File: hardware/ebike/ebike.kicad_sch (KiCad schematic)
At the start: 0 parts

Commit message: decoupling caps for STM
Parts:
- added C1, C2, C3, C7: 100n, symbol Device:C
- added C10, C9: 15p, symbol Device:C
- added C4: 4.7u, symbol Device:C
- added C5: 10n, symbol Device:C
- added C6, C8: 1u, symbol Device:C
- added FB1: 47, symbol Device:FerriteBead
- added U1: STM32G431CBTx, Package_QFP:LQFP-48_7x7mm_P0.5mm, symbol MCU_ST_STM32G4:STM32G431CBTx
- added Y1: ABLS-8MHZ-B2-T, E-Bike Footprints:XTAL_ABLS-8.000MHZ-B2-T, symbol Device:Crystal
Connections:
- new net: C5.1, C6.1, FB1.2
- new net: C10.1, U1.6 (PF1), Y1.2
- new net: C9.1, U1.5 (PF0), Y1.1
- new net +3.3V: C1.1, C2.1, C3.1, C4.1, C7.1, C8.1, FB1.1, U1.1 (VBAT), U1.20 (VREF+), U1.21 (VDDA), U1.24 (VDD), U1.36 (VDD), U1.48 (VDD)
- new net GND: C1.2, C10.2, C2.2, C3.2, C4.2, C5.2, C6.2, C7.2, C8.2, C9.2, U1.19 (VSSA), U1.23 (VSS), U1.35 (VSS), U1.47 (VSS)
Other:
- added sheet Battery Management (batteryman.kicad_sch)
- added sheet Motor Control (motor.kicad_sch)
- added sheet Peripherals (peripherals.kicad_sch)

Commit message: started on power management
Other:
- sheet Battery Management renamed Power Control
- added sheet Battery Control (battery_control.kicad_sch)
- sheet Power Control: file batteryman.kicad_sch -> power.kicad_sch
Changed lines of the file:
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@@
+	)
+	(sheet
+		(at 21.59 91.44)
+		(size 29.21 12.7)
+		(exclude_from_sim no)
+		(in_bom yes)
+		(on_board yes)
+		(dnp no)
+		(fields_autoplaced yes)
+		(stroke
+			(width 0.1524)
+			(type solid)
+		)
+		(fill
+			(color 0 0 0 0.0000)
+		)
+		(property "Sheetname" "Battery Control"
+			(at 21.59 90.7284 0)
+			(effects
+				(font
+					(size 1.27 1.27)
+				)
+				(justify left bottom)
+			)
+		)
+		(property "Sheetfile" "battery_control.kicad_sch"
+			(at 21.59 104.7246 0)
+			(effects
+				(font
+					(size 1.27 1.27)
+				)
+				(justify left top)
+			)
+		)
+		(instances
+			(project "ebike"
+				(path "/fbe3366b-3e6e-4322-b4fc-2801645ea115"
+					(page "5")
+				)
+			)
+		)
 	)
 	(sheet
@@
 			(color 0 0 0 0.0000)
 		)
-		(property "Sheetname" "Battery Management"
+		(property "Sheetname" "Power Control"
 			(at 21.59 51.3584 0)
 			(effects
@@
 			)
 		)
-		(property "Sheetfile" "batteryman.kicad_sch"
+		(property "Sheetfile" "power.kicad_sch"
 			(at 21.59 65.3546 0)
 			(effects

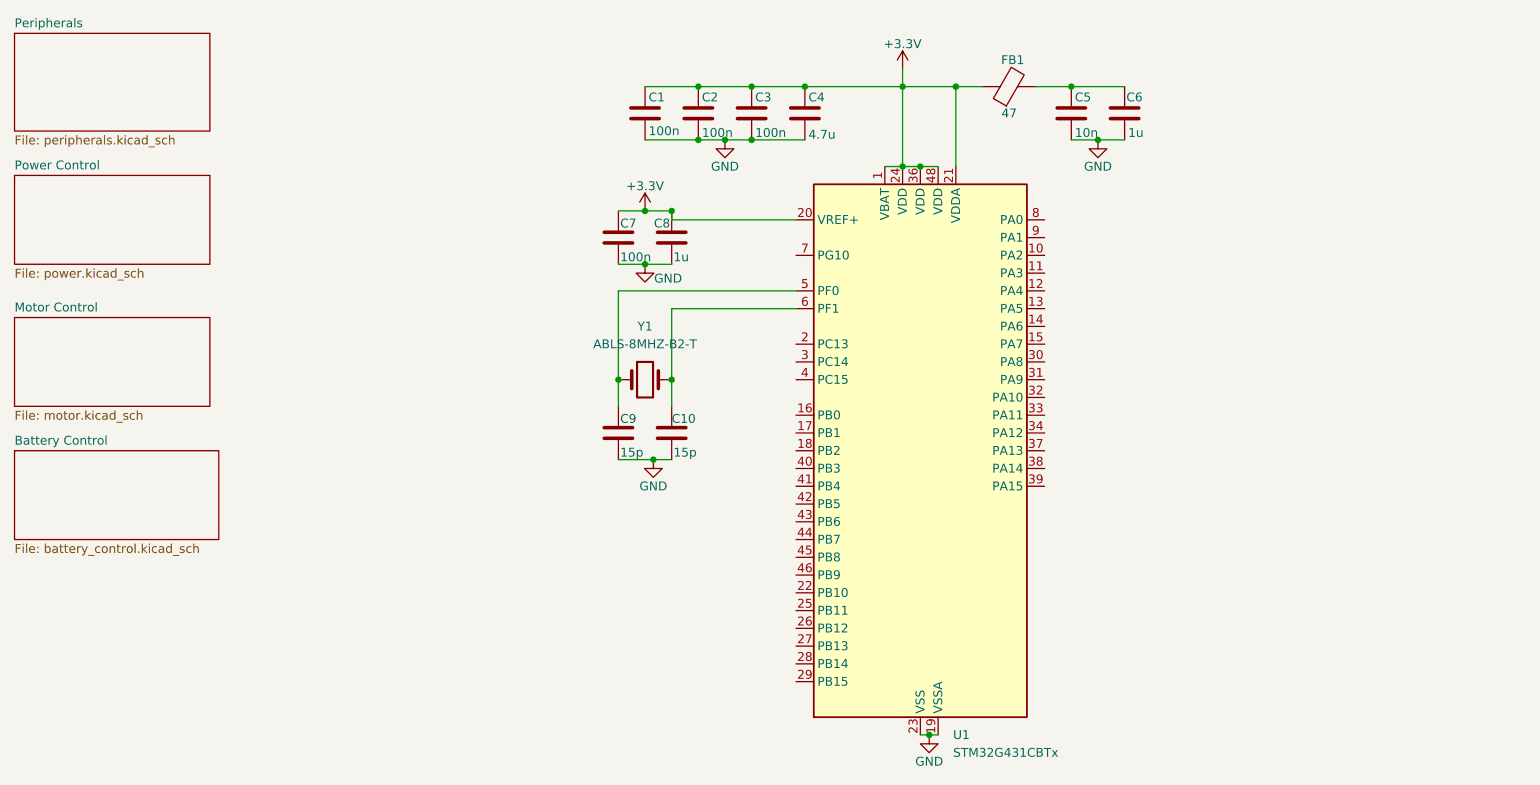
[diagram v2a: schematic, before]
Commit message: Wired PWM, ADC to MCU. Added HAL filtration + battery decoupling
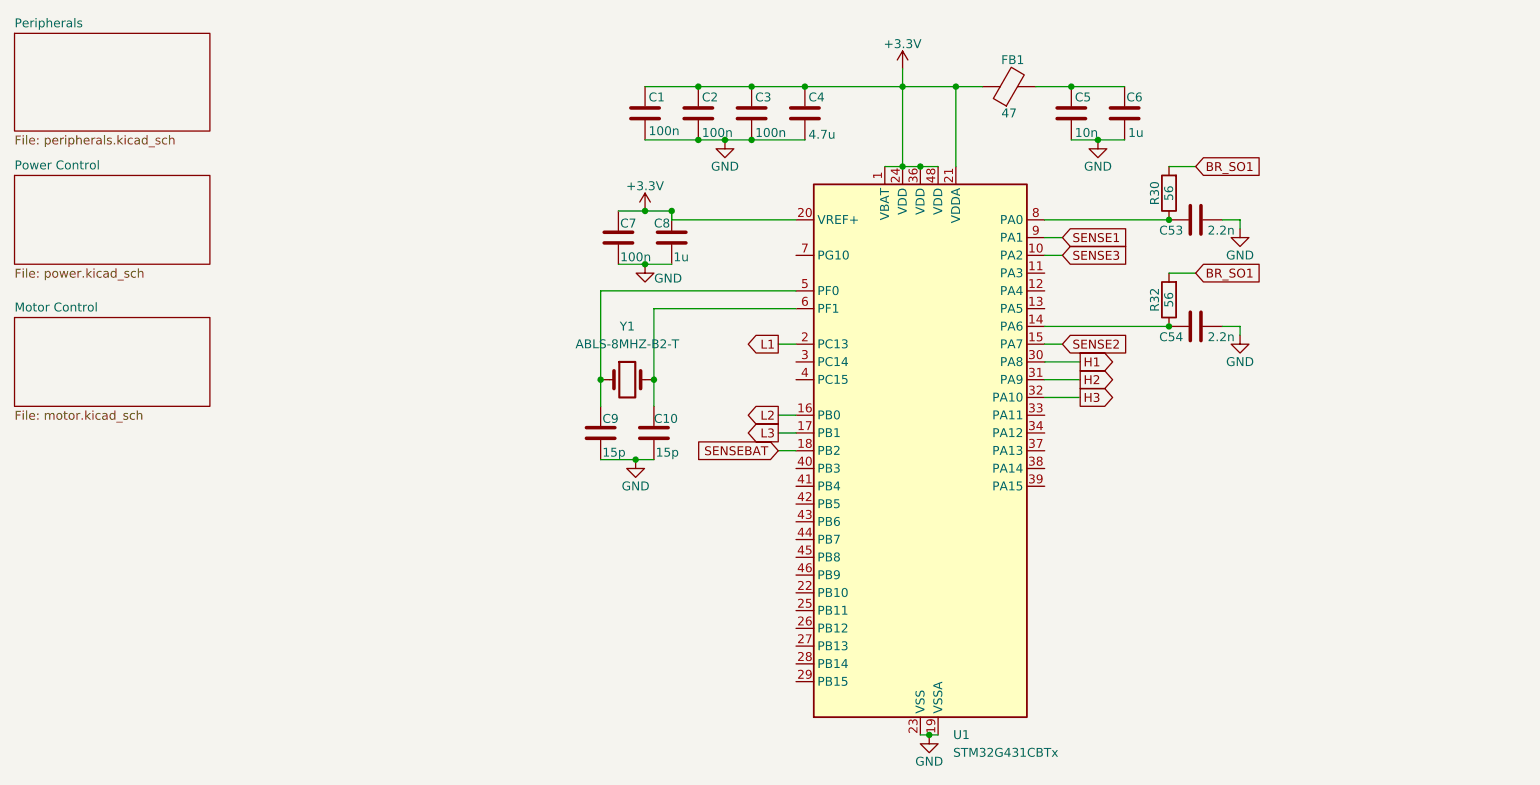
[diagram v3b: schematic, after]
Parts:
- added C53, C54: 2.2n, symbol Device:C
- added R30, R32: 56, symbol Device:R
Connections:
- net GND: now also C53.2, C54.2
- net SENSE3: now reaches U1.10 (PA2)
- net at U1.14 (PA6): now also C54.1, R32.1
- net SENSE2: now reaches U1.15 (PA7)
- net L2: now reaches U1.16 (PB0)
- net L3: now reaches U1.17 (PB1)
- net SENSEBAT: now reaches U1.18 (PB2)
- net L1: now reaches U1.2 (PC13)
- net H1: now reaches U1.30 (PA8)
- net H2: now reaches U1.31 (PA9)
- net H3: now reaches U1.32 (PA10)
- net at U1.8 (PA0): now also C53.1, R30.1
- net SENSE1: now reaches U1.9 (PA1)
- new net BR_SO1: R30.2, R32.2
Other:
- removed sheet Battery Control
- moved on the sheet: C10, C9, Y1

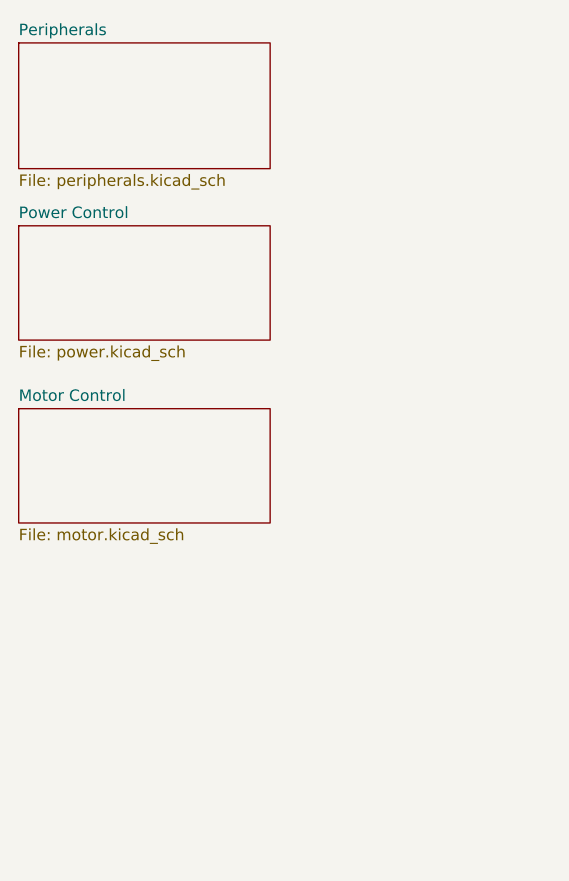
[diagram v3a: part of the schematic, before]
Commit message: wired most of peripherals
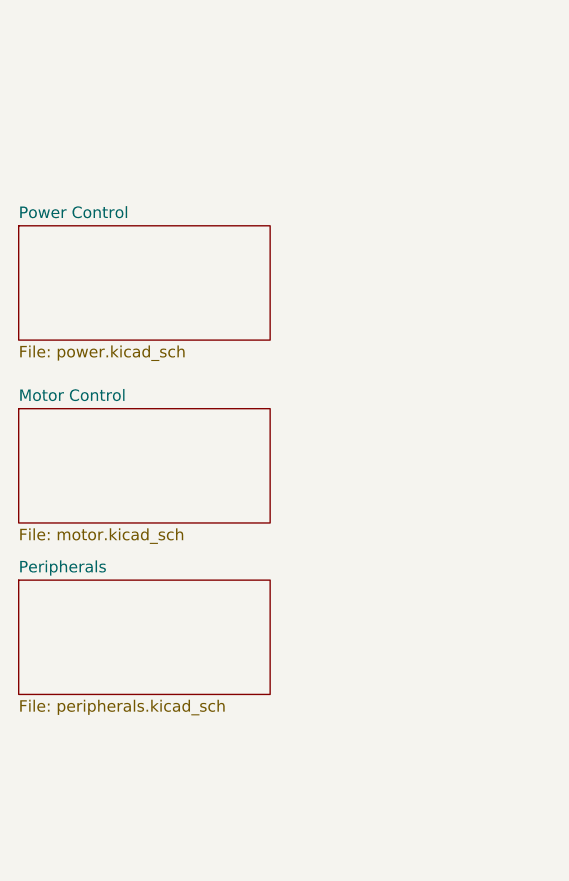
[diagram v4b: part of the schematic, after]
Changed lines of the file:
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@@
+	)
+	(sheet
+		(at 21.59 91.44)
+		(size 27.94 12.7)
+		(exclude_from_sim no)
+		(in_bom yes)
+		(on_board yes)
+		(dnp no)
+		(fields_autoplaced yes)
+		(stroke
+			(width 0.1524)
+			(type solid)
+		)
+		(fill
+			(color 0 0 0 0.0000)
+		)
+		(property "Sheetname" "Peripherals"
+			(at 21.59 90.7284 0)
+			(effects
+				(font
+					(size 1.27 1.27)
+				)
+				(justify left bottom)
+			)
+		)
+		(property "Sheetfile" "peripherals.kicad_sch"
+			(at 21.59 104.7246 0)
+			(effects
+				(font
+					(size 1.27 1.27)
+				)
+				(justify left top)
+			)
+		)
+		(instances
+			(project "ebike"
+				(path "/fbe3366b-3e6e-4322-b4fc-2801645ea115"
+					(page "4")
+				)
+			)
+		)
 	)
 	(sheet
@@
 			(project "ebike"
 				(path "/fbe3366b-3e6e-4322-b4fc-2801645ea115"
-					(page "4")
-				)
-			)
-		)
-	)
-	(sheet
-		(at 21.59 31.75)
-		(size 27.94 13.97)
-		(exclude_from_sim no)
-		(in_bom yes)
-		(on_board yes)
-		(dnp no)
-		(fields_autoplaced yes)
-		(stroke
-			(width 0.1524)
-			(type solid)
-		)
-		(fill
-			(color 0 0 0 0.0000)
-		)
-		(property "Sheetname" "Peripherals"
-			(at 21.59 31.0384 0)
-			(effects
-				(font
-					(size 1.27 1.27)
-				)
-				(justify left bottom)
-			)
-		)
-		(property "Sheetfile" "peripherals.kicad_sch"
-			(at 21.59 46.3046 0)
-			(effects
-				(font
-					(size 1.27 1.27)
-				)
-				(justify left top)
-			)
-		)
-		(instances
-			(project "ebike"
-				(path "/fbe3366b-3e6e-4322-b4fc-2801645ea115"
-					(page "2")
+					(page "3")
 				)
 			)
@@
 			(project "ebike"
 				(path "/fbe3366b-3e6e-4322-b4fc-2801645ea115"
-					(page "3")
+					(page "2")
 				)
 			)

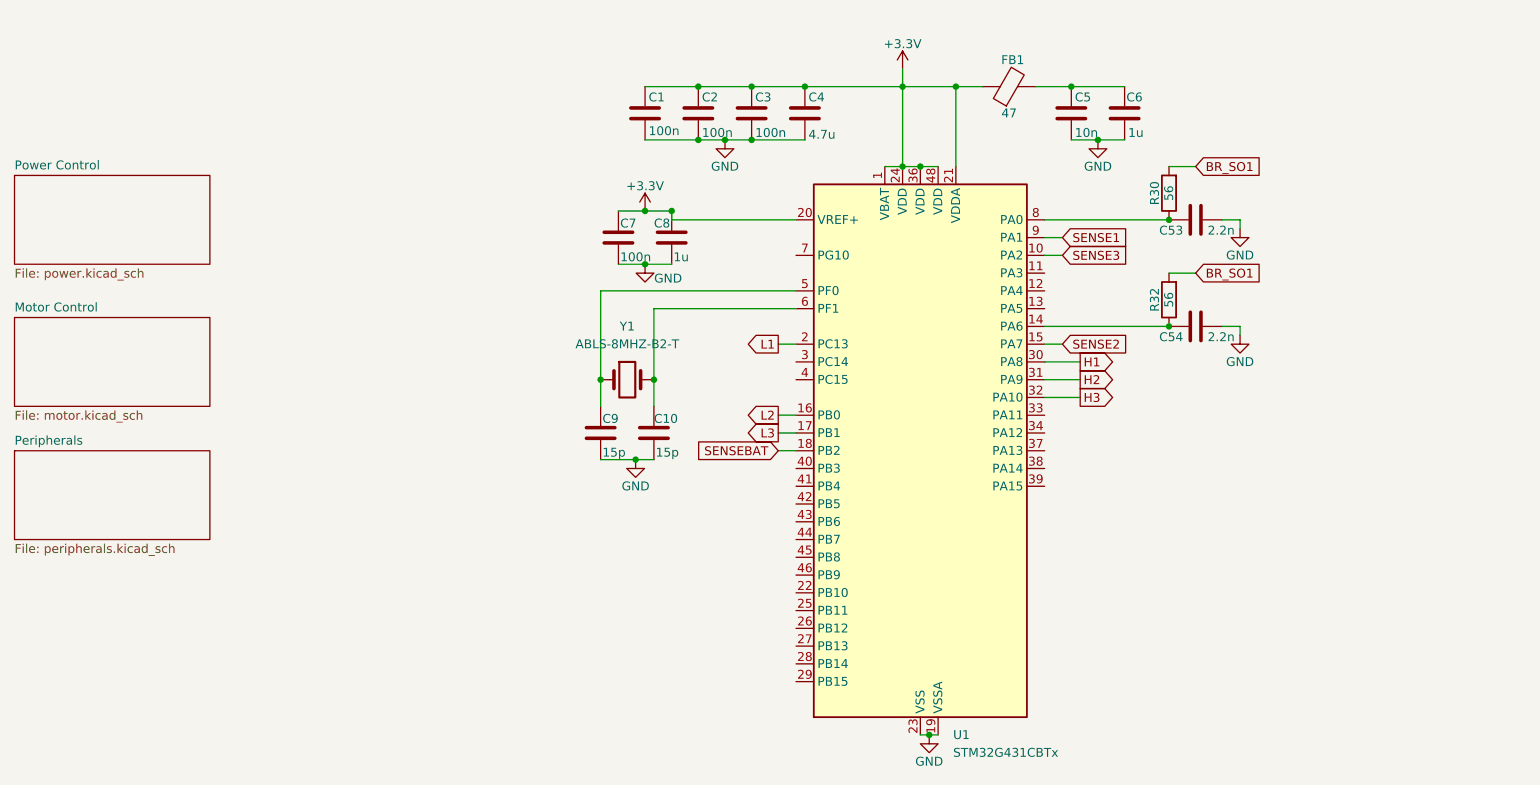
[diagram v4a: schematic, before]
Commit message: Added all peripherals and started modifying power circuitry
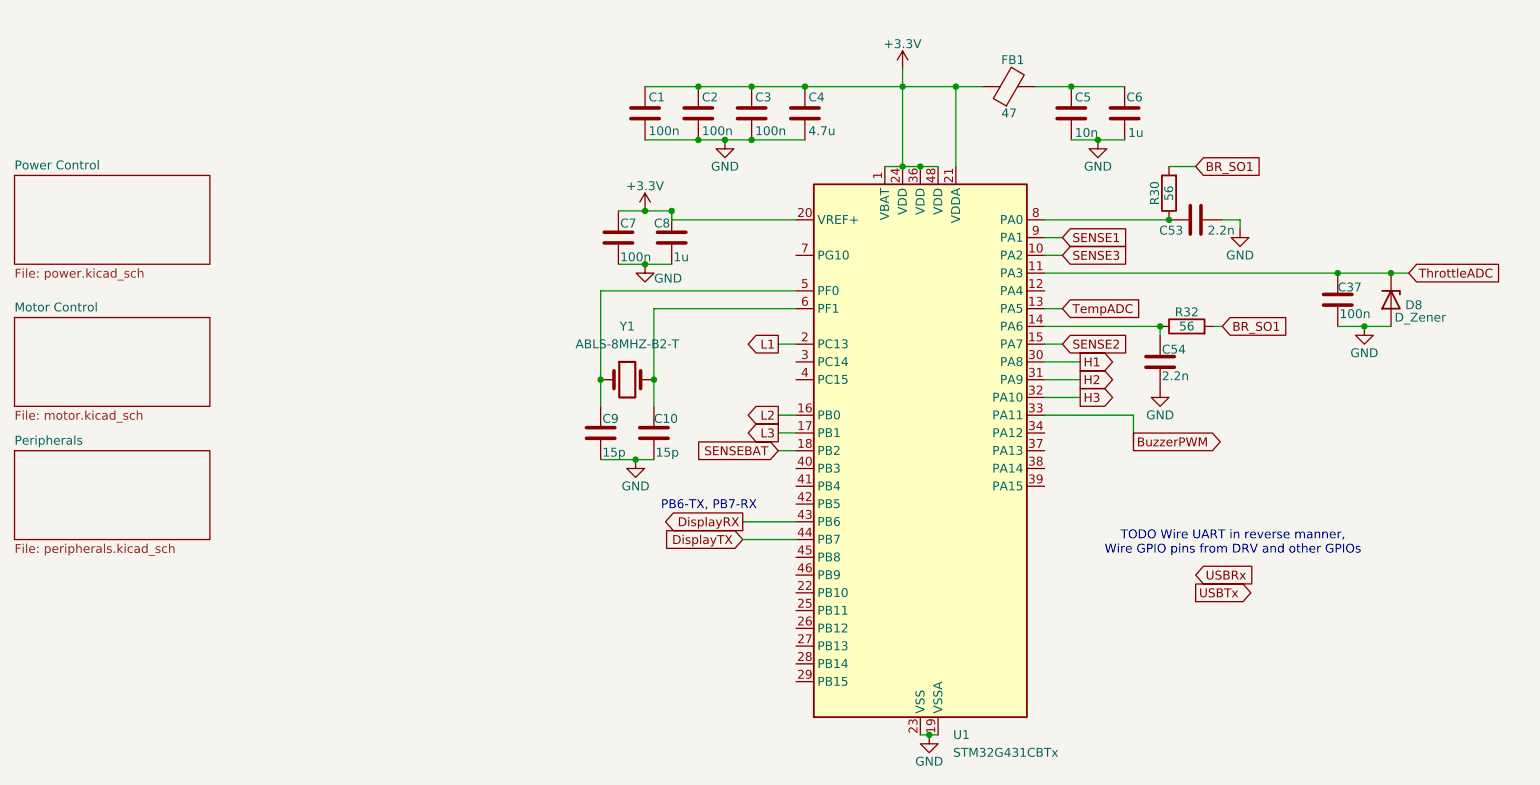
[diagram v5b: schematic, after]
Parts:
- added C37: 100n, symbol Device:C
- added D8: D_Zener, symbol Device:D_Zener
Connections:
- net GND: now also C37.2, D8.2 (A)
- net ThrottleADC: now reaches U1.11 (PA3)
- net ThrottleADC: now also C37.1, D8.1 (K)
- net TempADC: now reaches U1.13 (PA5)
- net BuzzerPWM: now reaches U1.33 (PA11)
- net DisplayRX: now reaches U1.43 (PB6)
- net DisplayTX: now reaches U1.44 (PB7)
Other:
- note added: "PB6-TX, PB7-RX"
- note added: "TODO Wire UART in reverse manner, Wire GPIO pins from DRV and other GPIOs"
- moved on the sheet: C54, R32

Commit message: schematic ready for first review
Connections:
- net BR_SO1: now also R30.1; no longer R30.2, R32.2
- net USBRx: now also U1.38 (PA14)
- net USBTx: now also U1.39 (PA15)
- net at C53.1, U1.8 (PA0): now also R30.2; no longer R30.1
- net HAL2: now reaches U1.22 (PB10)
- net HAL3: now reaches U1.25 (PB11)
- net LED1: now reaches U1.26 (PB12)
- net LED2: now reaches U1.27 (PB13)
- net FAULT: now reaches U1.40 (PB3)
- net DC_CAL: now reaches U1.41 (PB4)
- net EN_GATE: now reaches U1.42 (PB5)
- net HAL1: now reaches U1.46 (PB9)
- new net BR_SO2: R32.2
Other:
- note removed: "TODO Wire UART in reverse manner, Wire GPIO pins from DRV and other GPIOs"
- moved on the sheet: C54, R30

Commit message: working through first review, edited Power control a lot
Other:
- note added: "Route this"
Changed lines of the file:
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@@
+		)
+	)
+	(text "Route this\n"
+		(exclude_from_sim no)
+		(at 183.134 114.554 0)
+		(effects
+			(font
+				(size 1.27 1.27)
+			)
 		)
 	)
@@
 			(effects
 				(font
+					(size 1.27 1.27)
+				)
+				(justify right)
+				(hide yes)
+			)
+		)
+	)
+	(global_label "OCTW"
+		(shape input)
+		(at 186.69 116.84 180)
+		(fields_autoplaced yes)
+		(effects
+			(font
+				(size 1.27 1.27)
+			)
+			(justify right)
+		)
+		(property "Intersheetrefs" "${INTERSHEET_REFS}"
+			(at 178.6853 116.84 0)
+			(effects
+				(font

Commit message: finished annoation for schematic
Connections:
- net OCTW: now also U1.12 (PA4)
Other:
- note removed: "Route this"
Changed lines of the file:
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@@
-		)
-	)
-	(text "Route this\n"
-		(exclude_from_sim no)
-		(at 183.134 114.554 0)
-		(effects
-			(font
-				(size 1.27 1.27)
-			)
 		)
 	)
@@
 		(pts
 			(xy 184.15 77.47) (xy 182.88 77.47)
+		)
+		(stroke
+			(width 0)
+			(type default)
+		)
+	)
+	(wire
+		(pts
+			(xy 168.91 68.58) (xy 171.45 68.58)
 		)
 		(stroke
@@
 	(global_label "OCTW"
 		(shape input)
-		(at 186.69 116.84 180)
+		(at 171.45 68.58 0)
 		(fields_autoplaced yes)
 		(effects
@@
 				(size 1.27 1.27)
 			)
-			(justify right)
+			(justify left)
 		)
 		(property "Intersheetrefs" "${INTERSHEET_REFS}"
-			(at 178.6853 116.84 0)
+			(at 179.4547 68.58 0)
 			(effects
 				(font
 					(size 1.27 1.27)
 				)
-				(justify right)
+				(justify left)
 				(hide yes)
 			)
